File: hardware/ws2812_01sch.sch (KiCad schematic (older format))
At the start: 64 parts

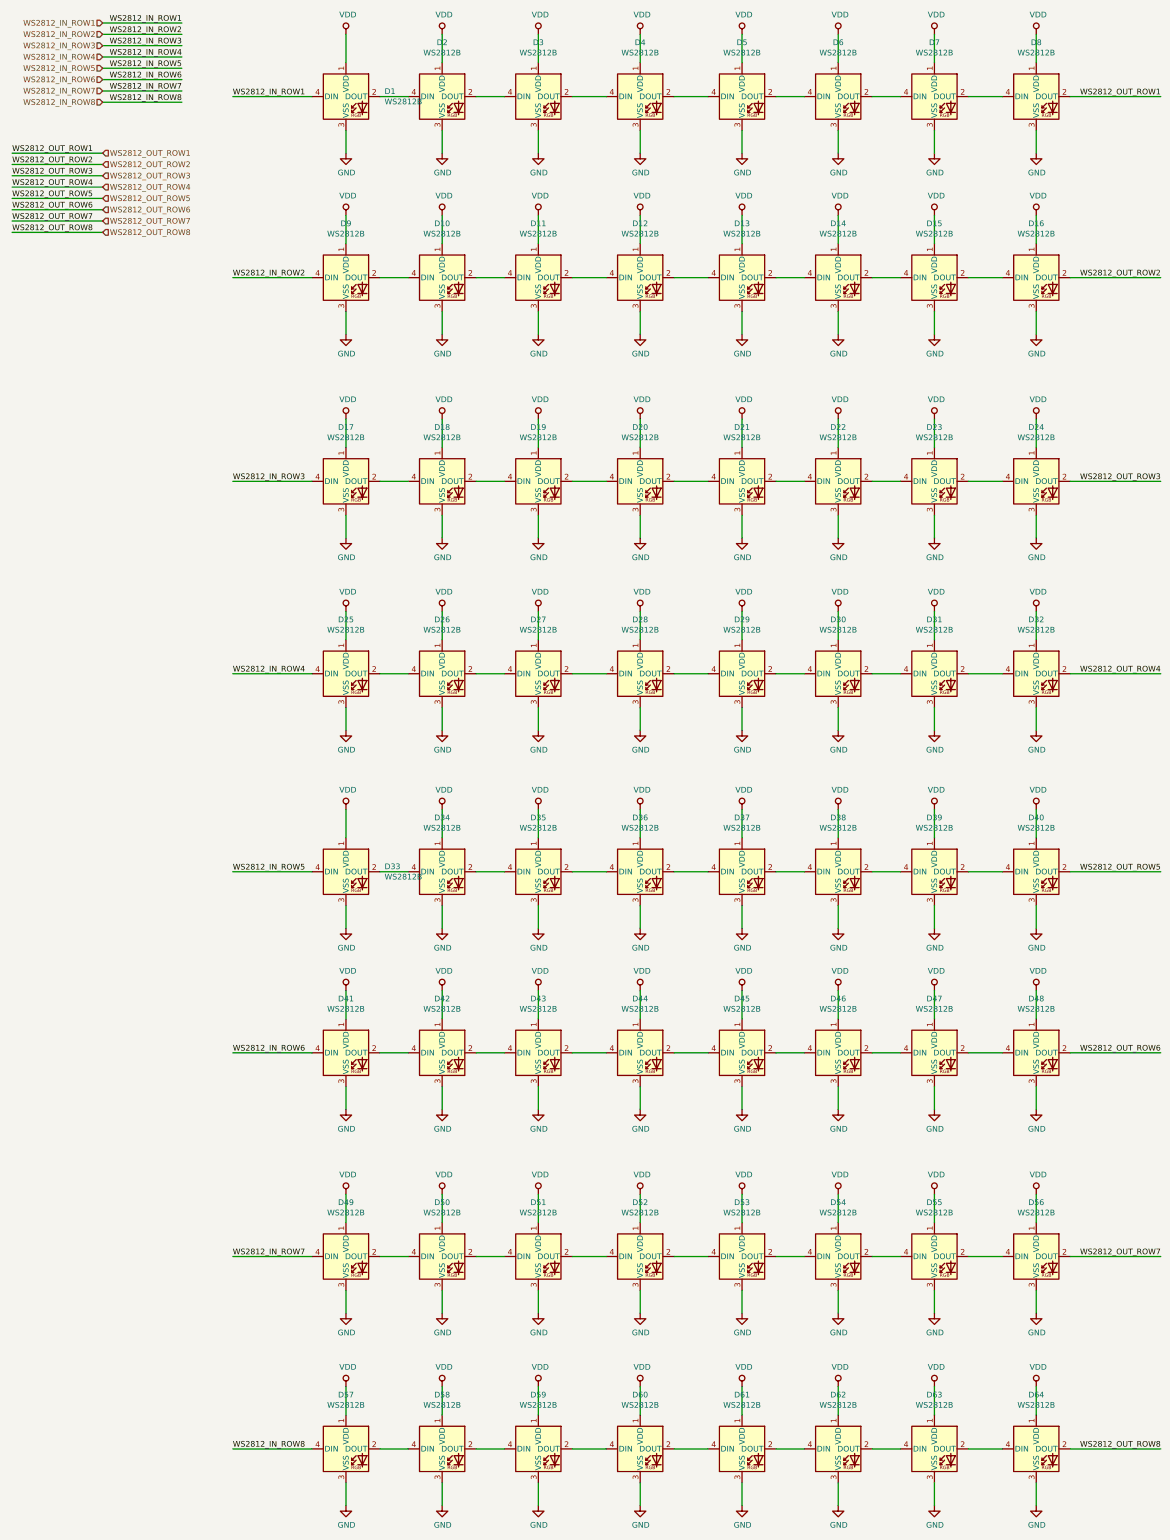
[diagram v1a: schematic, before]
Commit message: update WS2812\,
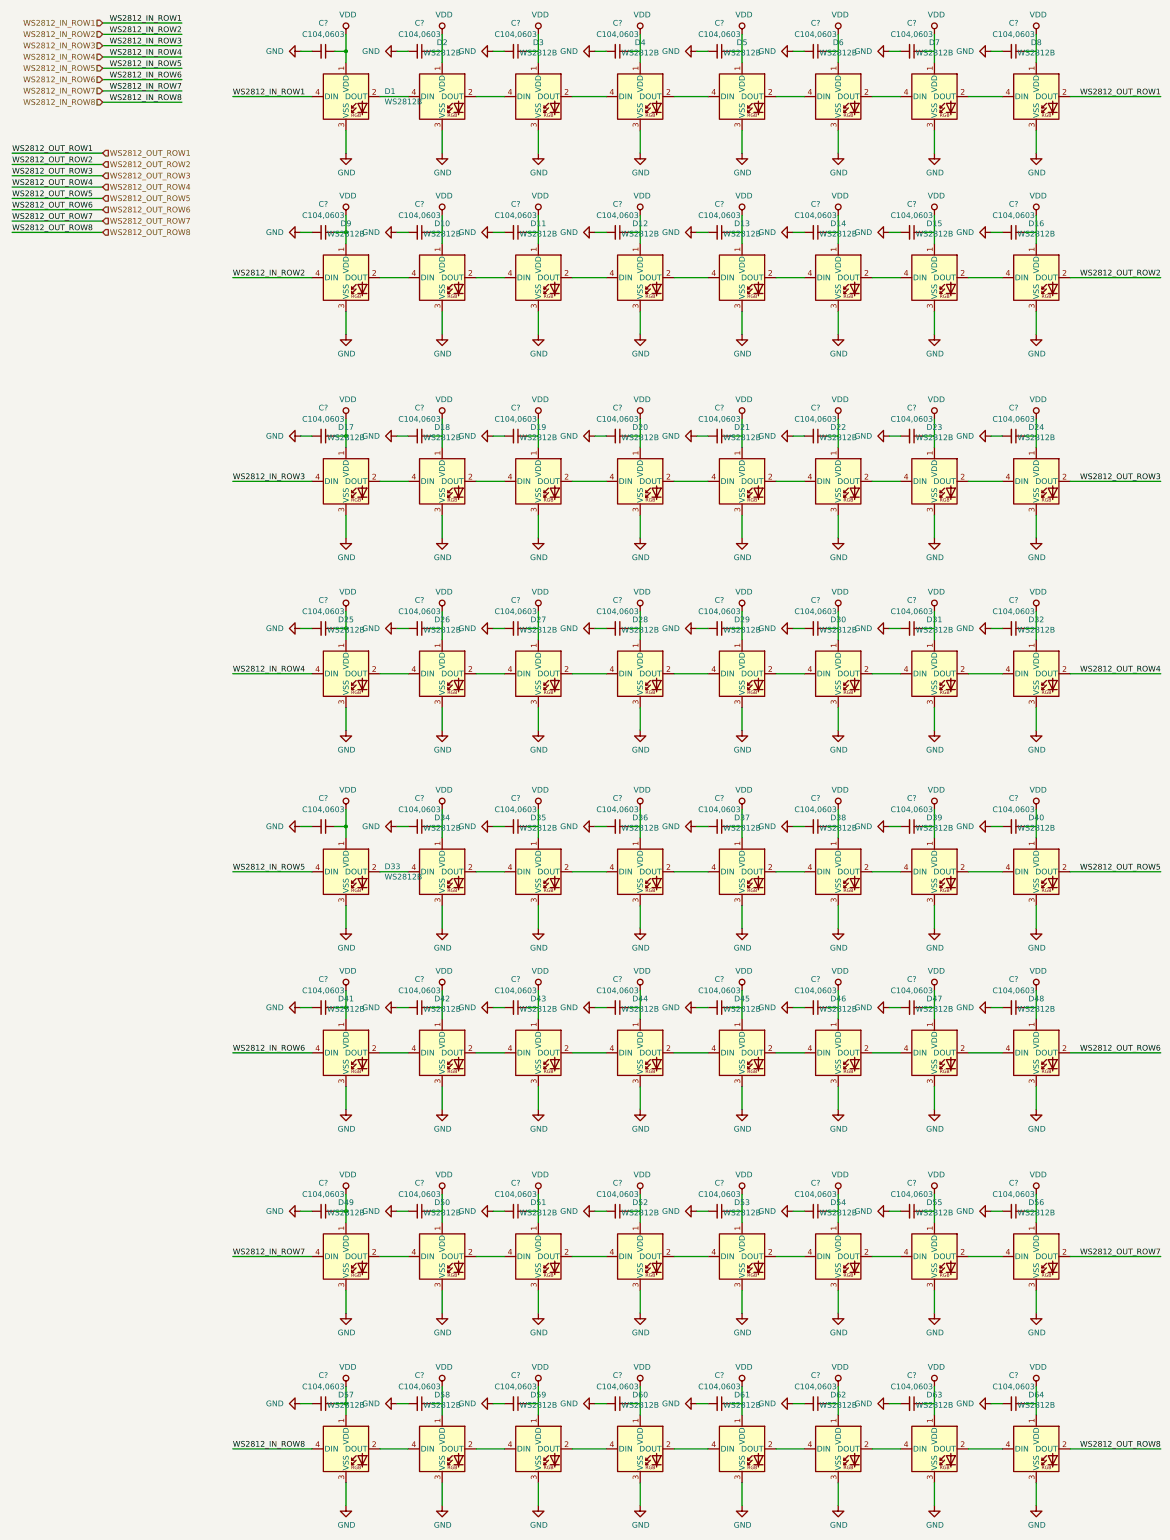
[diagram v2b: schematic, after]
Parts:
- added C? (x64): C104,0603, Capacitor_SMD:C_0603_1608Metric_Pad1.05x0.95mm_HandSolder, symbol taobao-c:C104,0603
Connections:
- wire segments 216 -> 352

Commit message: update WS2812\,
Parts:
- gave numbers to parts that had none: 64
